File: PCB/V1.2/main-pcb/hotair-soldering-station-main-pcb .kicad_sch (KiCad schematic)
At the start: 140 parts, among them J1 230VAC_IN, J10 T12_power (NS-25 r2,54), J11 LCD_CON2 (JST r.2.0), J12 LCD_CON1 (JST r.2.0), J13 ICP (goldpin r2,54), J14 Unused_GPIO, J2 FRONT_PANEL (IDC r. 2,54), J3 EARTH_GND, J4 24V_IN (NS-25 r2,54), J5 PSUPPLY (PWZ-02S r.3,96), J6 HOTAIR_FAN (JST r,2,54), J7 HOTAIR_MEAS (JST r.2,5), J8 HOTAIR_HEATER (PWZ-02S r.3,96), J9 WEP (r.2,54), Q1 BC817, Q10 RFP15P05, Q11 BC817, Q12 BC817, Q13 BC817, Q14 BC807, Q15 RFP15P05, Q2 BC807, Q3 BC817, Q4 RFP15P05, Q5 BC817, Q6 BT139-600, Q7 BC817, Q8 BC807, Q9 BC817, U1 MOC3041M, U2 MAX31855KASA, U3 MP1584-Step-Down, U4 AP1117-ADJ, U5 LM741, U6 AD8606, U8 STM32F103C6Tx

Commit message: Routing PCB
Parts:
- RV1: footprint Potentiometer_THT:Potentiometer_Bourns_3296W_Vertical -> Potentiometer_SMD:Potentiometer_Bourns_3314G_Vertical
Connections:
- net +3V3: now also R32.2
- net +5V: no longer R32.2, R53.2
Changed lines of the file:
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@@
     (pin "2")
-  )
-  (symbol (lib_id "power:+5V") (at 125.73 339.725 0) (unit 1)
-    (in_bom yes) (on_board yes)
-    (property "Reference" "#PWR0165" (id 0) (at 125.73 343.535 0)
-      (effects (font (size 1.27 1.27)) hide)
-    )
-    (property "Value" "+5V" (id 1) (at 126.111 335.3308 0))
-    (property "Footprint" "" (id 2) (at 125.73 339.725 0)
-      (effects (font (size 1.27 1.27)) hide)
-    )
-    (property "Datasheet" "" (id 3) (at 125.73 339.725 0)
-      (effects (font (size 1.27 1.27)) hide)
-    )
-    (pin "1")
   )
   (symbol (lib_id "Amplifier_Operational:LM741") (at 252.73 353.06 0) (unit 1)
@@
     (pin "~")
   )
+  (symbol (lib_id "power:+3.3V") (at 125.73 339.725 0) (unit 1)
+    (in_bom yes) (on_board yes)
+    (property "Reference" "#PWR0120" (id 0) (at 125.73 343.535 0)
+      (effects (font (size 1.27 1.27)) hide)
+    )
+    (property "Value" "+3.3V" (id 1) (at 126.111 335.3308 0))
+    (property "Footprint" "" (id 2) (at 125.73 339.725 0)
+      (effects (font (size 1.27 1.27)) hide)
+    )
+    (property "Datasheet" "" (id 3) (at 125.73 339.725 0)
+      (effects (font (size 1.27 1.27)) hide)
+    )
+    (pin "1")
+  )
   (symbol (lib_id "Device:R") (at 65.405 239.395 180) (unit 1)
     (in_bom yes) (on_board yes)
@@
     (property "Reference" "RV1" (id 0) (at 259.842 364.998 90))
     (property "Value" "10k" (id 1) (at 259.842 367.03 90))
-    (property "Footprint" "Potentiometer_THT:Potentiometer_Bourns_3296W_Vertical" (id 2) (at 260.096 369.316 0)
+    (property "Footprint" "Potentiometer_SMD:Potentiometer_Bourns_3314G_Vertical" (id 2) (at 260.096 369.316 0)
       (effects (font (size 1.27 1.27)) hide)
     )
@@
     (pin "1")
     (pin "2")
-  )
-  (symbol (lib_id "power:+5V") (at 405.765 281.94 0) (unit 1)
-    (in_bom yes) (on_board yes)
-    (property "Reference" "#PWR0120" (id 0) (at 405.765 285.75 0)
-      (effects (font (size 1.27 1.27)) hide)
-    )
-    (property "Value" "+5V" (id 1) (at 406.146 277.5458 0))
-    (property "Footprint" "" (id 2) (at 405.765 281.94 0)
-      (effects (font (size 1.27 1.27)) hide)
-    )
-    (property "Datasheet" "" (id 3) (at 405.765 281.94 0)
-      (effects (font (size 1.27 1.27)) hide)
-    )
-    (pin "1")
   )
   (symbol (lib_id "Device:R") (at 352.425 250.19 90) (mirror x) (unit 1)
@@
     (pin "2")
   )
+  (symbol (lib_id "power:+3.3V") (at 405.13 281.94 0) (unit 1)
+    (in_bom yes) (on_board yes)
+    (property "Reference" "#PWR0110" (id 0) (at 405.13 285.75 0)
+      (effects (font (size 1.27 1.27)) hide)
+    )
+    (property "Value" "+3.3V" (id 1) (at 405.511 277.5458 0))
+    (property "Footprint" "" (id 2) (at 405.13 281.94 0)
+      (effects (font (size 1.27 1.27)) hide)
+    )
+    (property "Datasheet" "" (id 3) (at 405.13 281.94 0)
+      (effects (font (size 1.27 1.27)) hide)
+    )
+    (pin "1")
+  )
   (symbol (lib_id "Device:R") (at 67.945 304.8 90) (mirror x) (unit 1)
     (in_bom yes) (on_board yes)
@@
       (reference "#PWR0109") (unit 1) (value "+24V") (footprint "")
     )
+    (path "/d150ceb9-17a4-4723-af81-fa40df62506e"
+      (reference "#PWR0110") (unit 1) (value "+3.3V") (footprint "")
+    )
     (path "/00000000-0000-0000-0000-00005f80ab4c"
       (reference "#PWR0111") (unit 1) (value "GND") (footprint "")
@@
       (reference "#PWR0119") (unit 1) (value "GND") (footprint "")
     )
-    (path "/9d01e559-2b65-408d-a9ff-919c0dffcc1c"
-      (reference "#PWR0120") (unit 1) (value "+5V") (footprint "")
+    (path "/77fbec0c-38d6-4731-ae1c-d577d3c1cc17"
+      (reference "#PWR0120") (unit 1) (value "+3.3V") (footprint "")
     )
     (path "/00000000-0000-0000-0000-000060efe55c"
@@
       (reference "#PWR0164") (unit 1) (value "GND") (footprint "")
     )
-    (path "/060f4c52-2491-4554-b2a3-cbbe53dc762a"
-      (reference "#PWR0165") (unit 1) (value "+5V") (footprint "")
-    )
     (path "/937cc063-504b-42e3-9e62-4c4eebdbb4da"
       (reference "#PWR0166") (unit 1) (value "GND") (footprint "")
@@
     )
     (path "/8ebb3e1c-a0d2-4947-9e86-d7f8729cc0af"
-      (reference "RV1") (unit 1) (value "10k") (footprint "Potentiometer_THT:Potentiometer_Bourns_3296W_Vertical")
+      (reference "RV1") (unit 1) (value "10k") (footprint "Potentiometer_SMD:Potentiometer_Bourns_3314G_Vertical")
     )
     (path "/00000000-0000-0000-0000-00005f7da3cf"

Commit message: Routing PCB
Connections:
- net +3V3: now also R53.2
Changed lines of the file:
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@@
     (pin "2")
     (pin "3")
-  )
-  (symbol (lib_id "SparkFun-IC-Amplifiers:LM358") (at 383.54 247.65 0) (unit 2)
-    (in_bom yes) (on_board yes)
-    (property "Reference" "U6" (id 0) (at 383.54 238.6584 0)
-      (effects (font (size 1.143 1.143)))
-    )
-    (property "Value" "AD8606" (id 1) (at 383.54 240.792 0)
-      (effects (font (size 1.143 1.143)))
-    )
-    (property "Footprint" "Package_SO:SO-8_3.9x4.9mm_P1.27mm" (id 2) (at 383.54 238.76 0)
-      (effects (font (size 0.508 0.508)) hide)
-    )
-    (property "Datasheet" "" (id 3) (at 383.54 247.65 0)
-      (effects (font (size 1.27 1.27)) hide)
-    )
-    (property "Pole4" "IC-09172" (id 4) (at 383.54 240.5126 0)
-      (effects (font (size 1.524 1.524)) hide)
-    )
     (pin "5")
     (pin "6")
     (pin "7")
+    (pin "4")
+    (pin "8")
+  )
+  (symbol (lib_id "SparkFun-IC-Amplifiers:LM358") (at 383.54 247.65 0) (unit 2)
+    (in_bom yes) (on_board yes)
+    (property "Reference" "U6" (id 0) (at 383.54 238.6584 0)
+      (effects (font (size 1.143 1.143)))
+    )
+    (property "Value" "AD8606" (id 1) (at 383.54 240.792 0)
+      (effects (font (size 1.143 1.143)))
+    )
+    (property "Footprint" "Package_SO:SO-8_3.9x4.9mm_P1.27mm" (id 2) (at 383.54 238.76 0)
+      (effects (font (size 0.508 0.508)) hide)
+    )
+    (property "Datasheet" "" (id 3) (at 383.54 247.65 0)
+      (effects (font (size 1.27 1.27)) hide)
+    )
+    (property "Pole4" "IC-09172" (id 4) (at 383.54 240.5126 0)
+      (effects (font (size 1.524 1.524)) hide)
+    )
+    (pin "1")
+    (pin "2")
+    (pin "3")
+    (pin "5")
+    (pin "6")
+    (pin "7")
+    (pin "4")
+    (pin "8")
   )
   (symbol (lib_id "SparkFun-IC-Amplifiers:LM358") (at 421.64 227.965 0) (unit 3)
@@
       (effects (font (size 1.524 1.524)) (justify left) hide)
     )
+    (pin "1")
+    (pin "2")
+    (pin "3")
+    (pin "5")
+    (pin "6")
+    (pin "7")
     (pin "4")
     (pin "8")
@@
     (pin "2")
   )
-  (symbol (lib_id "power:+3.3V") (at 405.13 281.94 0) (unit 1)
-    (in_bom yes) (on_board yes)
-    (property "Reference" "#PWR0110" (id 0) (at 405.13 285.75 0)
-      (effects (font (size 1.27 1.27)) hide)
-    )
-    (property "Value" "+3.3V" (id 1) (at 405.511 277.5458 0))
-    (property "Footprint" "" (id 2) (at 405.13 281.94 0)
-      (effects (font (size 1.27 1.27)) hide)
-    )
-    (property "Datasheet" "" (id 3) (at 405.13 281.94 0)
-      (effects (font (size 1.27 1.27)) hide)
-    )
+  (symbol (lib_id "power:+3.3V") (at 405.765 281.94 0) (unit 1)
+    (in_bom yes) (on_board yes)
+    (property "Reference" "#PWR0110" (id 0) (at 405.765 285.75 0)
+      (effects (font (size 1.27 1.27)) hide)
+    )
+    (property "Value" "+3.3V" (id 1) (at 406.146 277.5458 0))
+    (property "Footprint" "" (id 2) (at 405.765 281.94 0)
+      (effects (font (size 1.27 1.27)) hide)
+    )
+    (property "Datasheet" "" (id 3) (at 405.765 281.94 0)
+      (effects (font (size 1.27 1.27)) hide)
+    )

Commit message: Routing PCB done, resolving DRC violations
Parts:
- J14: footprint My-Footprints:WIRE_PAD_1,3mm -> Wire_Pads:SolderWirePad_single_0-8mmDrill
- Q13, Q5: footprint Package_TO_SOT_SMD:SOT-23 -> Package_TO_SOT_SMD:TSOT-23
- R27: footprint Resistor_THT:R_Axial_DIN0204_L3.6mm_D1.6mm_P1.90mm_Vertical -> My-Footprints:ShortWire
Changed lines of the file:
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@@
       (effects (font (size 1.27 1.27)) (justify right))
     )
-    (property "Footprint" "Resistor_THT:R_Axial_DIN0204_L3.6mm_D1.6mm_P1.90mm_Vertical" (id 2) (at 292.1 201.168 90)
+    (property "Footprint" "My-Footprints:ShortWire" (id 2) (at 292.1 201.168 90)
       (effects (font (size 1.27 1.27)) hide)
     )
@@
     (pin "2")
     (pin "3")
-    (pin "5")
-    (pin "6")
-    (pin "7")
-    (pin "4")
-    (pin "8")
   )
   (symbol (lib_id "SparkFun-IC-Amplifiers:LM358") (at 383.54 247.65 0) (unit 2)
@@
       (effects (font (size 1.524 1.524)) hide)
     )
-    (pin "1")
-    (pin "2")
-    (pin "3")
     (pin "5")
     (pin "6")
     (pin "7")
-    (pin "4")
-    (pin "8")
   )
   (symbol (lib_id "SparkFun-IC-Amplifiers:LM358") (at 421.64 227.965 0) (unit 3)
@@
       (effects (font (size 1.524 1.524)) (justify left) hide)
     )
-    (pin "1")
-    (pin "2")
-    (pin "3")
-    (pin "5")
-    (pin "6")
-    (pin "7")
     (pin "4")
     (pin "8")
@@
       (effects (font (size 1.27 1.27)) (justify left))
     )
-    (property "Footprint" "Package_TO_SOT_SMD:SOT-23" (id 2) (at 382.905 173.355 0)
+    (property "Footprint" "Package_TO_SOT_SMD:TSOT-23" (id 2) (at 382.905 173.355 0)
       (effects (font (size 1.27 1.27) italic) (justify left) hide)
     )
@@
       (effects (font (size 1.27 1.27)) (justify left))
     )
-    (property "Footprint" "My-Footprints:WIRE_PAD_1,3mm" (id 2) (at 560.705 297.815 0)
+    (property "Footprint" "Wire_Pads:SolderWirePad_single_0-8mmDrill" (id 2) (at 560.705 297.815 0)
       (effects (font (size 1.27 1.27)) hide)
     )
@@
       (effects (font (size 1.27 1.27)) (justify left))
     )
-    (property "Footprint" "Package_TO_SOT_SMD:SOT-23" (id 2) (at 243.84 171.45 0)
+    (property "Footprint" "Package_TO_SOT_SMD:TSOT-23" (id 2) (at 243.84 171.45 0)
       (effects (font (size 1.27 1.27) italic) (justify left) hide)
     )
@@
     )
     (path "/914a350b-a7d7-4c79-a92d-ba59afbc607b"
-      (reference "J14") (unit 1) (value "Unused_GPIO") (footprint "My-Footprints:WIRE_PAD_1,3mm")
+      (reference "J14") (unit 1) (value "Unused_GPIO") (footprint "Wire_Pads:SolderWirePad_single_0-8mmDrill")
     )
     (path "/00000000-0000-0000-0000-00005fa04b60"
@@
     )
     (path "/f4dce22c-56d1-479a-b241-869dfa9e53bc"
-      (reference "Q5") (unit 1) (value "BC817") (footprint "Package_TO_SOT_SMD:SOT-23")
+      (reference "Q5") (unit 1) (value "BC817") (footprint "Package_TO_SOT_SMD:TSOT-23")
     )
     (path "/00000000-0000-0000-0000-00005f7ee591"
@@
     )
     (path "/2a3d044c-197b-4358-adfa-34da324497c5"
-      (reference "Q13") (unit 1) (value "BC817") (footprint "Package_TO_SOT_SMD:SOT-23")
+      (reference "Q13") (unit 1) (value "BC817") (footprint "Package_TO_SOT_SMD:TSOT-23")
     )
     (path "/65a5530f-1abc-4b78-b3db-c9f0b32235be"
@@
     )
     (path "/00000000-0000-0000-0000-00005f80d0dd"
-      (reference "R27") (unit 1) (value "0R") (footprint "Resistor_THT:R_Axial_DIN0204_L3.6mm_D1.6mm_P1.90mm_Vertical")
+      (reference "R27") (unit 1) (value "0R") (footprint "My-Footprints:ShortWire")
     )
     (path "/ba05b909-30fa-4e4e-a631-3d1ee3ebe47f"

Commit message: Silkscreen progress
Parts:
- C12: value 100n -> (none); footprint Capacitors:0603 -> (none)
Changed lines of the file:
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@@
     (pin "2")
     (pin "3")
-  )
-  (symbol (lib_id "SparkFun-IC-Amplifiers:LM358") (at 383.54 247.65 0) (unit 2)
-    (in_bom yes) (on_board yes)
-    (property "Reference" "U6" (id 0) (at 383.54 238.6584 0)
-      (effects (font (size 1.143 1.143)))
-    )
-    (property "Value" "AD8606" (id 1) (at 383.54 240.792 0)
-      (effects (font (size 1.143 1.143)))
-    )
-    (property "Footprint" "Package_SO:SO-8_3.9x4.9mm_P1.27mm" (id 2) (at 383.54 238.76 0)
-      (effects (font (size 0.508 0.508)) hide)
-    )
-    (property "Datasheet" "" (id 3) (at 383.54 247.65 0)
-      (effects (font (size 1.27 1.27)) hide)
-    )
-    (property "Pole4" "IC-09172" (id 4) (at 383.54 240.5126 0)
-      (effects (font (size 1.524 1.524)) hide)
-    )
     (pin "5")
     (pin "6")
     (pin "7")
+    (pin "4")
+    (pin "8")
+  )
+  (symbol (lib_id "SparkFun-IC-Amplifiers:LM358") (at 383.54 247.65 0) (unit 2)
+    (in_bom yes) (on_board yes)
+    (property "Reference" "U6" (id 0) (at 383.54 238.6584 0)
+      (effects (font (size 1.143 1.143)))
+    )
+    (property "Value" "AD8606" (id 1) (at 383.54 240.792 0)
+      (effects (font (size 1.143 1.143)))
+    )
+    (property "Footprint" "Package_SO:SO-8_3.9x4.9mm_P1.27mm" (id 2) (at 383.54 238.76 0)
+      (effects (font (size 0.508 0.508)) hide)
+    )
+    (property "Datasheet" "" (id 3) (at 383.54 247.65 0)
+      (effects (font (size 1.27 1.27)) hide)
+    )
+    (property "Pole4" "IC-09172" (id 4) (at 383.54 240.5126 0)
+      (effects (font (size 1.524 1.524)) hide)
+    )
+    (pin "1")
+    (pin "2")
+    (pin "3")
+    (pin "5")
+    (pin "6")
+    (pin "7")
+    (pin "4")
+    (pin "8")
   )
   (symbol (lib_id "SparkFun-IC-Amplifiers:LM358") (at 421.64 227.965 0) (unit 3)
@@
       (effects (font (size 1.524 1.524)) (justify left) hide)
     )
+    (pin "1")
+    (pin "2")
+    (pin "3")
+    (pin "5")
+    (pin "6")
+    (pin "7")
     (pin "4")
     (pin "8")
@@
       (effects (font (size 0.889 0.889)) (justify left))
     )
-    (property "Value" "100n" (id 1) (at 495.3 158.115 0)
+    (property "Value" "" (id 1) (at 495.3 158.115 0)
       (effects (font (size 0.889 0.889)) (justify left))
     )
-    (property "Footprint" "Capacitors:0603" (id 2) (at 495.6302 163.83 0)
+    (property "Footprint" "" (id 2) (at 495.6302 163.83 0)
       (effects (font (size 1.27 1.27)) hide)
     )
@@
     )
     (path "/00000000-0000-0000-0000-0000619cb12f"
-      (reference "C12") (unit 1) (value "100n") (footprint "Capacitors:0603")
+      (reference "C12") (unit 1) (value "100n") (footprint "Capacitors:0805")
     )
     (path "/00000000-0000-0000-0000-0000619cb5f7"

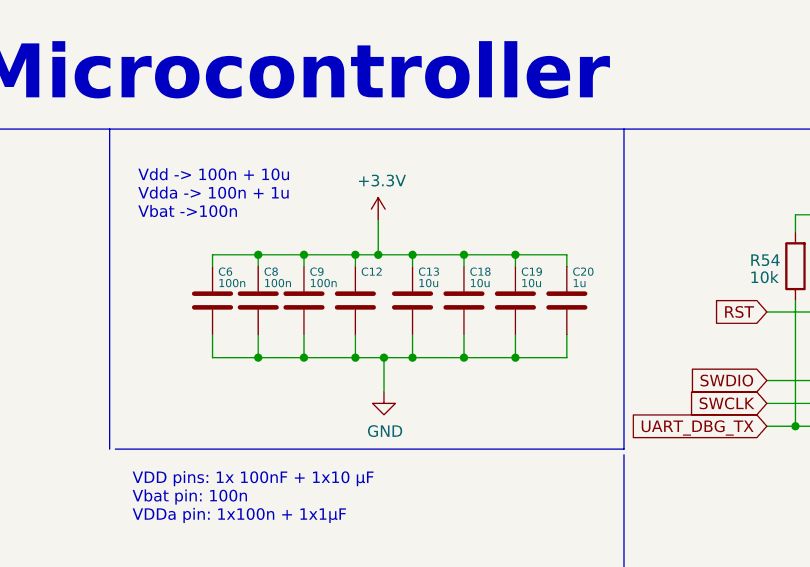
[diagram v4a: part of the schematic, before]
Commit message: Front panel rocker switch connector change, preparing pcb for production
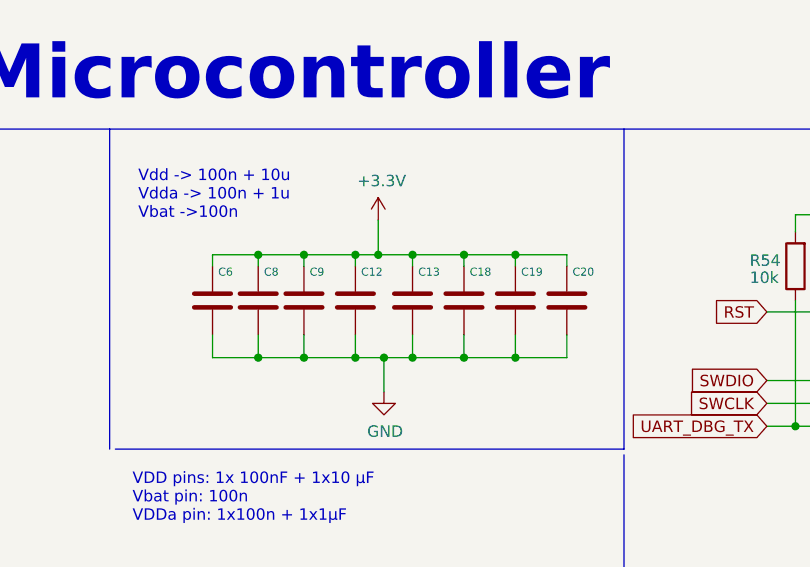
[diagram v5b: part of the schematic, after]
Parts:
- C13, C18, C19: value 10u -> (none); footprint Capacitors:0603 -> (none)
- C20: value 1u -> (none); footprint Capacitors:0603 -> (none)
- C6, C8: value 100n -> (none); footprint Capacitors:0603 -> (none)
- C9: value 100n -> (none); footprint Capacitor_SMD:C_0603_1608Metric -> (none)
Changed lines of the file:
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@@
       (effects (font (size 0.889 0.889)) (justify left))
     )
-    (property "Value" "100n" (id 1) (at 479.425 158.115 0)
+    (property "Value" "" (id 1) (at 479.425 158.115 0)
       (effects (font (size 0.889 0.889)) (justify left))
     )
-    (property "Footprint" "Capacitors:0603" (id 2) (at 479.7552 163.83 0)
+    (property "Footprint" "" (id 2) (at 479.7552 163.83 0)
       (effects (font (size 1.27 1.27)) hide)
     )
@@
       (effects (font (size 0.889 0.889)) (justify left))
     )
-    (property "Value" "100n" (id 1) (at 484.505 158.115 0)
+    (property "Value" "" (id 1) (at 484.505 158.115 0)
       (effects (font (size 0.889 0.889)) (justify left))
     )
-    (property "Footprint" "Capacitors:0603" (id 2) (at 484.8352 163.83 0)
+    (property "Footprint" "" (id 2) (at 484.8352 163.83 0)
       (effects (font (size 1.27 1.27)) hide)
     )
@@
       (effects (font (size 0.889 0.889)) (justify left))
     )
-    (property "Value" "100n" (id 1) (at 489.585 158.115 0)
+    (property "Value" "" (id 1) (at 489.585 158.115 0)
       (effects (font (size 0.889 0.889)) (justify left))
     )
-    (property "Footprint" "Capacitor_SMD:C_0603_1608Metric" (id 2) (at 489.9152 163.83 0)
+    (property "Footprint" "" (id 2) (at 489.9152 163.83 0)
       (effects (font (size 1.27 1.27)) hide)
     )
@@
       (effects (font (size 0.889 0.889)) (justify left))
     )
-    (property "Value" "10u" (id 1) (at 501.65 158.115 0)
+    (property "Value" "" (id 1) (at 501.65 158.115 0)
       (effects (font (size 0.889 0.889)) (justify left))
     )
-    (property "Footprint" "Capacitors:0603" (id 2) (at 501.9802 163.83 0)
+    (property "Footprint" "" (id 2) (at 501.9802 163.83 0)
       (effects (font (size 1.27 1.27)) hide)
     )
@@
       (effects (font (size 0.889 0.889)) (justify left))
     )
-    (property "Value" "10u" (id 1) (at 507.365 158.115 0)
+    (property "Value" "" (id 1) (at 507.365 158.115 0)
       (effects (font (size 0.889 0.889)) (justify left))
     )
-    (property "Footprint" "Capacitors:0603" (id 2) (at 507.6952 163.83 0)
+    (property "Footprint" "" (id 2) (at 507.6952 163.83 0)
       (effects (font (size 1.27 1.27)) hide)
     )
@@
       (effects (font (size 0.889 0.889)) (justify left))
     )
-    (property "Value" "10u" (id 1) (at 513.08 158.115 0)
+    (property "Value" "" (id 1) (at 513.08 158.115 0)
       (effects (font (size 0.889 0.889)) (justify left))
     )
-    (property "Footprint" "Capacitors:0603" (id 2) (at 513.4102 163.83 0)
+    (property "Footprint" "" (id 2) (at 513.4102 163.83 0)
       (effects (font (size 1.27 1.27)) hide)
     )
@@
       (effects (font (size 0.889 0.889)) (justify left))
     )
-    (property "Value" "1u" (id 1) (at 518.795 158.115 0)
+    (property "Value" "" (id 1) (at 518.795 158.115 0)
       (effects (font (size 0.889 0.889)) (justify left))
     )
-    (property "Footprint" "Capacitors:0603" (id 2) (at 519.1252 163.83 0)
+    (property "Footprint" "" (id 2) (at 519.1252 163.83 0)
       (effects (font (size 1.27 1.27)) hide)
     )
@@
     )
     (path "/00000000-0000-0000-0000-00006190d725"
-      (reference "C6") (unit 1) (value "100n") (footprint "Capacitors:0603")
+      (reference "C6") (unit 1) (value "100n") (footprint "Capacitors:0805")
     )
     (path "/00000000-0000-0000-0000-00005f7faa2a"
@@
     )
     (path "/00000000-0000-0000-0000-00006190da9a"
-      (reference "C8") (unit 1) (value "100n") (footprint "Capacitors:0603")
+      (reference "C8") (unit 1) (value "100n") (footprint "Capacitors:0805")
     )
     (path "/00000000-0000-0000-0000-00006190dd47"
-      (reference "C9") (unit 1) (value "100n") (footprint "Capacitor_SMD:C_0603_1608Metric")
+      (reference "C9") (unit 1) (value "100n") (footprint "Capacitors:0805")
     )
     (path "/00000000-0000-0000-0000-00005f869f08"
@@
     )
     (path "/00000000-0000-0000-0000-0000619cb5f7"
-      (reference "C13") (unit 1) (value "10u") (footprint "Capacitors:0603")
+      (reference "C13") (unit 1) (value "10u") (footprint "Capacitors:0805")
     )
     (path "/00000000-0000-0000-0000-00005f8484e7"
@@
     )
     (path "/00000000-0000-0000-0000-0000619cc019"
-      (reference "C18") (unit 1) (value "10u") (footprint "Capacitors:0603")
+      (reference "C18") (unit 1) (value "10u") (footprint "Capacitors:0805")
     )
     (path "/00000000-0000-0000-0000-0000619cc3ed"
-      (reference "C19") (unit 1) (value "10u") (footprint "Capacitors:0603")
+      (reference "C19") (unit 1) (value "10u") (footprint "Capacitors:0805")
     )
     (path "/00000000-0000-0000-0000-0000619cc662"
-      (reference "C20") (unit 1) (value "1u") (footprint "Capacitors:0603")
+      (reference "C20") (unit 1) (value "1u") (footprint "Capacitors:0805")
     )
     (path "/d550ffd4-71b1-46ca-b0ec-99476bc498a4"
